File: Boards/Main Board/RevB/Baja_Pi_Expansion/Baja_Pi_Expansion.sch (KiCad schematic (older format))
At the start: 13 parts, among them J1 Conn_02x10_Counter_Clockwise, J2 Conn_02x12_Counter_Clockwise, J3 Screw_Terminal_01x04, J4 Conn_02x20_Odd_Even, J5 Conn_01x03_Male, J6 Screw_Terminal_01x07, U1 HDSP-7403

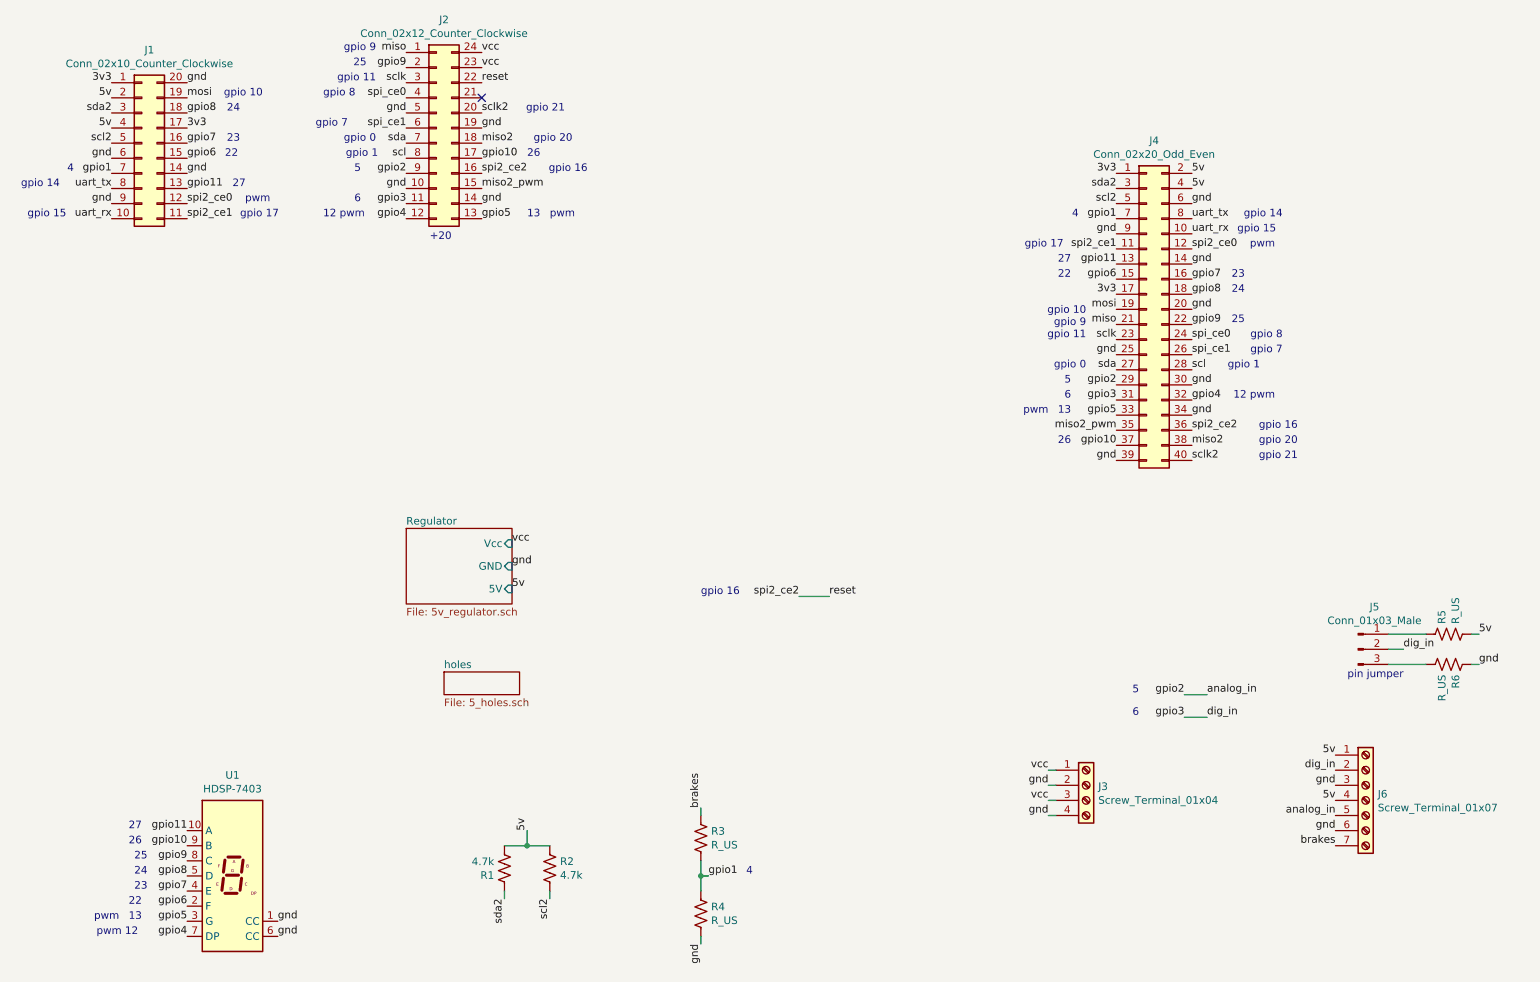
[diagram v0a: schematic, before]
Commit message: Updated Main Board RevB to reflect recent changes
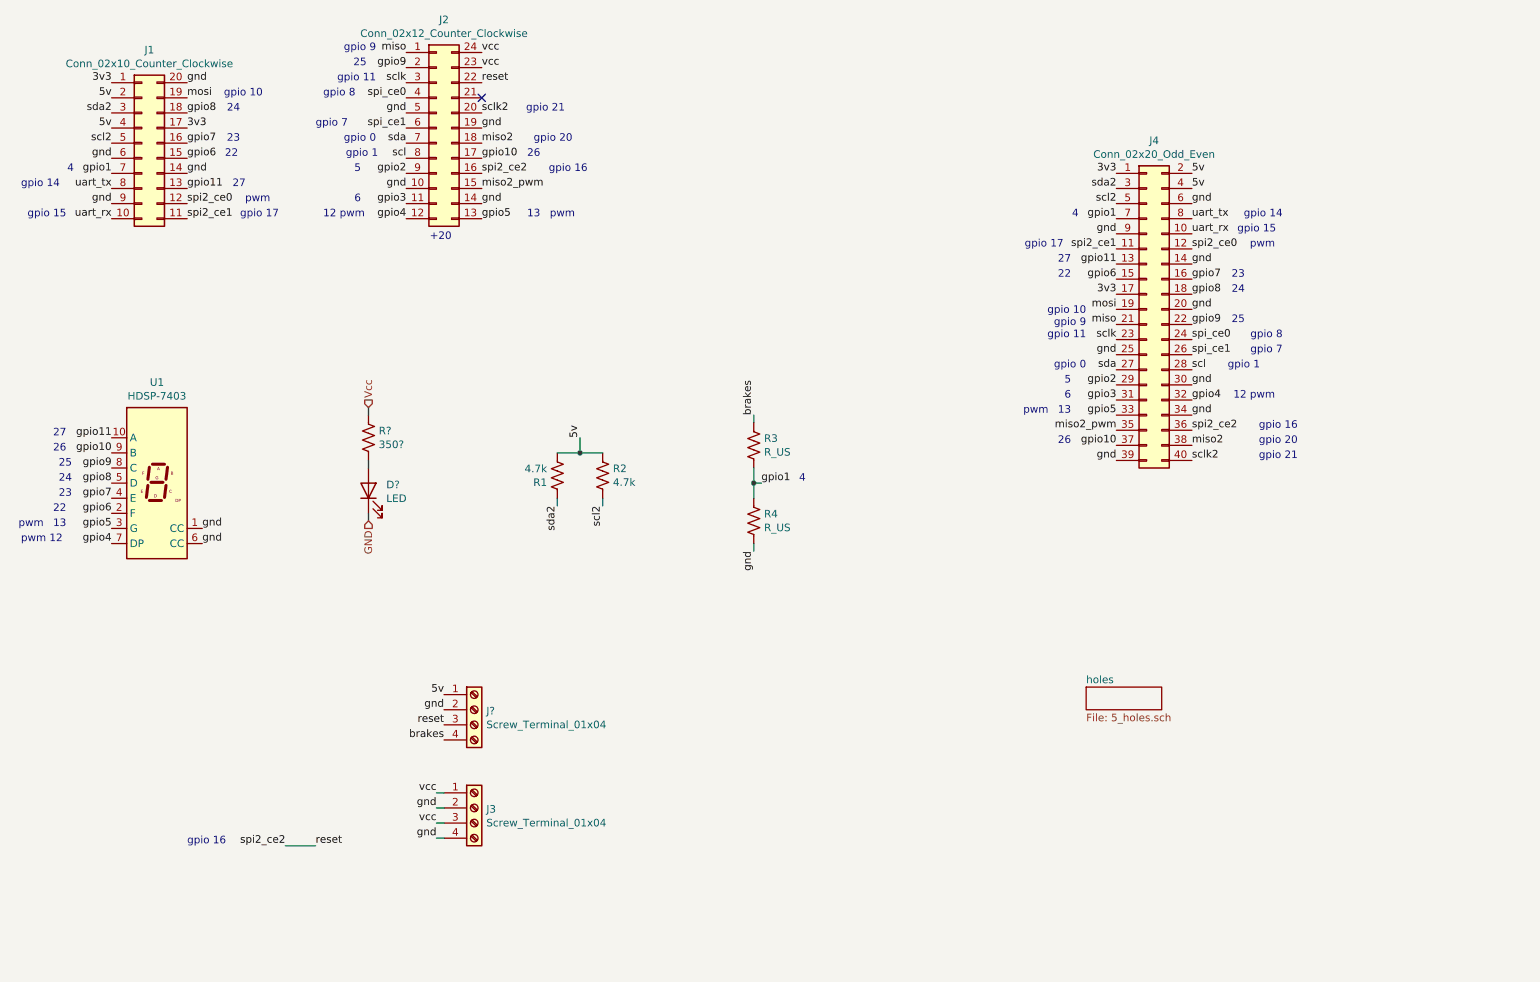
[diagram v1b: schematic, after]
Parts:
- removed J5: Conn_01x03_Male, Connector_PinHeader_2.54mm:PinHeader_1x03_P2.54mm_Vertical, symbol Connector:Conn_01x03_Male
- removed J6: Screw_Terminal_01x07, Connector_PinHeader_2.54mm:PinHeader_1x07_P2.54mm_Vertical, symbol Connector:Screw_Terminal_01x07
- removed R5, R6: R_US, Resistor_SMD:R_0603_1608Metric, symbol Device:R_US
- added D?: LED, LED_SMD:LED_1812_4532Metric, symbol Device:LED
- added J?: Screw_Terminal_01x04, Connector_PinHeader_2.54mm:PinHeader_1x04_P2.54mm_Vertical, symbol Connector:Screw_Terminal_01x04
- added R?: 350?, Resistor_SMD:R_0603_1608Metric, symbol Device:R_US
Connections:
- net 5v: now also J?.1 (Pin_1)
- net brakes: now also J?.4 (Pin_4)
- net gnd: now also J?.2 (Pin_2)
- net reset: now also J?.3 (Pin_3)
- net analog_in renamed gpio2
- net dig_in renamed gpio3
- new net: D?.2 (A), R?.2
- new net GND: D?.1 (K)
- new net Vcc: R?.1
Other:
- note removed: "pin jumper"
- moved on the sheet: J3, R1, R2, R3, R4, U1

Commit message: Updated Main-RevB annotations and added placeholder for Breadboard_Testbed
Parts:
- gave numbers to parts that had none: 3
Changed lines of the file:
@@
 $EndComp
 $Comp
-L Device:R_US R?
+L Device:R_US R5
 U 1 1 61FC7A2D
 P 3400 3700
-AR Path="/61FC7A2D" Ref="R?"  Part="1"
+AR Path="/61FC7A2D" Ref="R5"  Part="1"
 AR Path="/6164E083/61FC7A2D" Ref="R?"  Part="1"
-F 0 "R?" H 3468 3746 50  0000 L CNN
+F 0 "R5" H 3468 3746 50  0000 L CNN
 F 1 "350?" H 3468 3655 50  0000 L CNN
 F 2 "Resistor_SMD:R_0603_1608Metric" V 3440 3690 50  0001 C CNN
@@
 $EndComp
 $Comp
-L Device:LED D?
+L Device:LED D1
 U 1 1 61FC7A33
 P 3400 4050
-AR Path="/61FC7A33" Ref="D?"  Part="1"
+AR Path="/61FC7A33" Ref="D1"  Part="1"
 AR Path="/6164E083/61FC7A33" Ref="D?"  Part="1"
-F 0 "D?" V 3439 3932 50  0000 R CNN
+F 0 "D1" V 3439 3932 50  0000 R CNN
 F 1 "LED" V 3348 3932 50  0000 R CNN
 F 2 "LED_SMD:LED_1812_4532Metric" H 3400 4050 50  0001 C CNN
@@
 	3400 3500 3400 3550
 $Comp
-L Connector:Screw_Terminal_01x04 J?
+L Connector:Screw_Terminal_01x04 J5
 U 1 1 61FCA862
 P 4100 5500
-F 0 "J?" H 4180 5492 50  0000 L CNN
+F 0 "J5" H 4180 5492 50  0000 L CNN
 F 1 "Screw_Terminal_01x04" H 4180 5401 50  0000 L CNN
 F 2 "Connector_PinHeader_2.54mm:PinHeader_1x04_P2.54mm_Vertical" H 4100 5500 50  0001 C CNN

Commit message: Main-RevB Pre-route complete. Waiting on footprint confirmation
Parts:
- J3, J5: footprint Connector_PinHeader_2.54mm:PinHeader_1x04_P2.54mm_Vertical -> Custom Footprints:Spring_4
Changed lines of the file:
@@
 F 0 "J3" H 4180 6142 50  0000 L CNN
 F 1 "Screw_Terminal_01x04" H 4180 6051 50  0000 L CNN
-F 2 "Connector_PinHeader_2.54mm:PinHeader_1x04_P2.54mm_Vertical" H 4100 6150 50  0001 C CNN
+F 2 "Custom Footprints:Spring_4" H 4100 6150 50  0001 C CNN
 F 3 "~" H 4100 6150 50  0001 C CNN
 	1    4100 6150
@@
 F 0 "J5" H 4180 5492 50  0000 L CNN
 F 1 "Screw_Terminal_01x04" H 4180 5401 50  0000 L CNN
-F 2 "Connector_PinHeader_2.54mm:PinHeader_1x04_P2.54mm_Vertical" H 4100 5500 50  0001 C CNN
+F 2 "Custom Footprints:Spring_4" H 4100 5500 50  0001 C CNN
 F 3 "~" H 4100 5500 50  0001 C CNN
 	1    4100 5500
